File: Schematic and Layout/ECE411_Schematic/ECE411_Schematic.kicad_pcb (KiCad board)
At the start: 2 copper layers, 65 x 56 mm, 13 parts, among them J1 Raspberry Pi GPIO, M1 Motor_DC, U2 PCF8574, U3 LM386, U4 L293D Driver

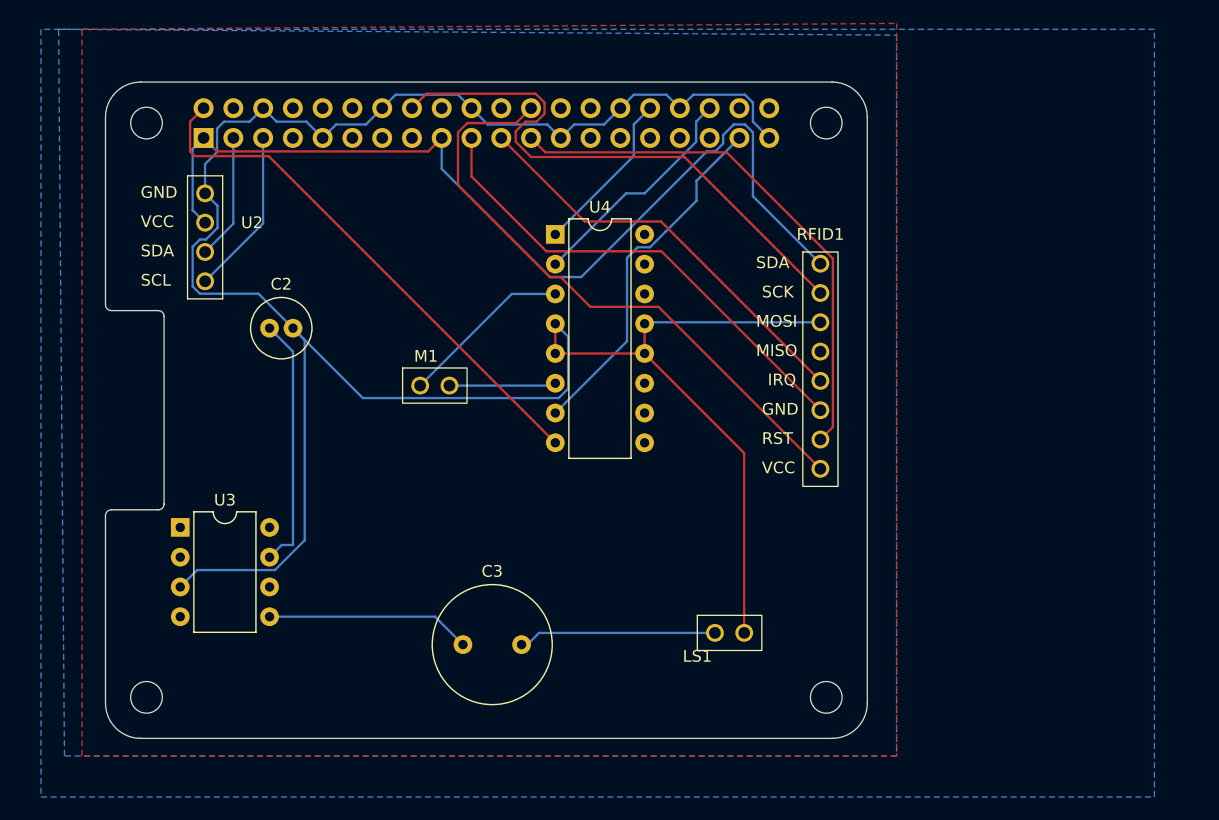
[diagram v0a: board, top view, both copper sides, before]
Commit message: added LEDs to indicate functioning subsystems
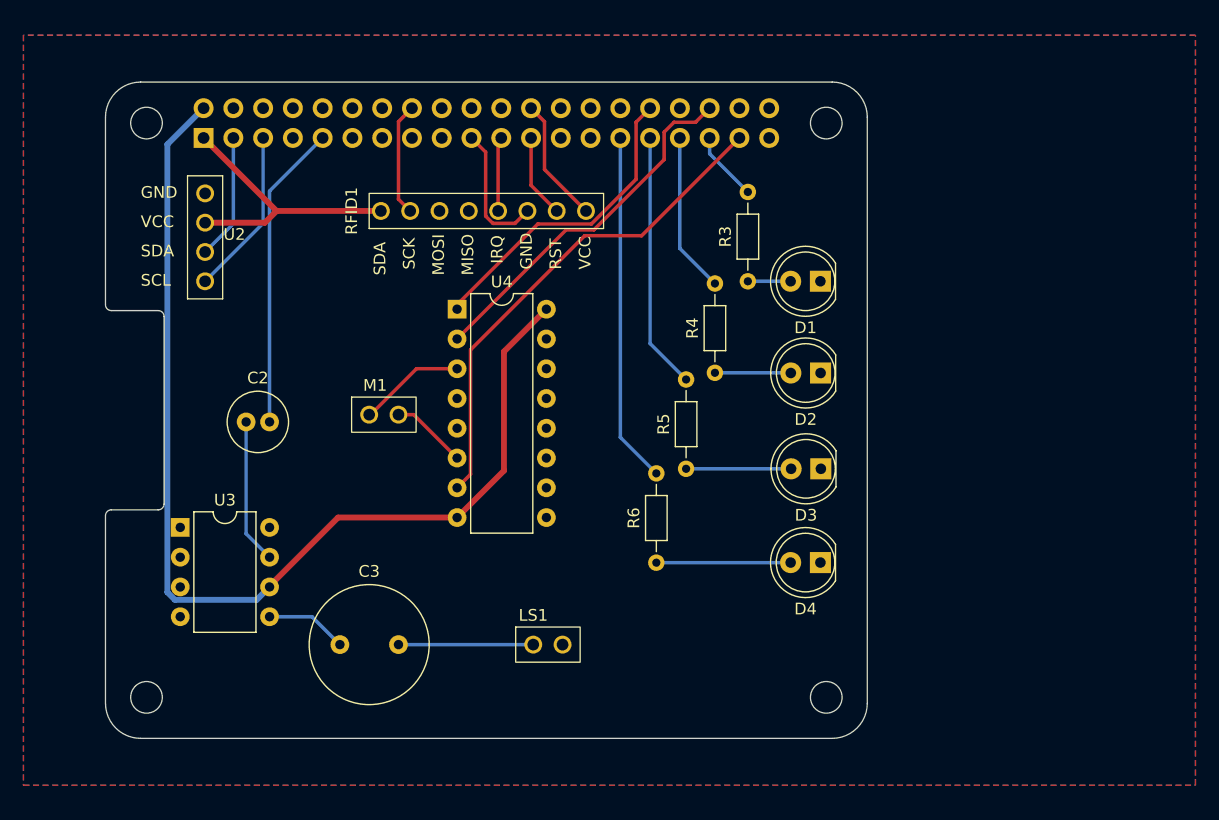
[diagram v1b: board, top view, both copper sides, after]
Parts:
- added D1: RFID LED, LED_THT:LED_D5.0mm, F.Cu at (161.0, 61.0)
- added D2: Motor LED, LED_THT:LED_D5.0mm, F.Cu at (161.0, 68.8)
- added D3: Speaker LED, LED_THT:LED_D5.0mm, F.Cu at (161.0, 77.0)
- added D4: Display LED, LED_THT:LED_D5.0mm, F.Cu at (161.0, 85.0)
- added R3: 220, Resistor_THT:R_Axial_DIN0204_L3.6mm_D1.6mm_P7.62mm_Horizontal, F.Cu at (154.8, 61.0)
- added R4: 220, Resistor_THT:R_Axial_DIN0204_L3.6mm_D1.6mm_P7.62mm_Horizontal, F.Cu at (152.0, 68.8)
- added R5: 220, Resistor_THT:R_Axial_DIN0204_L3.6mm_D1.6mm_P7.62mm_Horizontal, F.Cu at (149.5, 77.0)
- added R6: 220, Resistor_THT:R_Axial_DIN0204_L3.6mm_D1.6mm_P7.62mm_Horizontal, F.Cu at (147.0, 85.0)
- moved RFID1 26.4 mm to (142.5, 57.5), turned to 90 degrees
- moved LS1 15.5 mm to (135.0, 93.5)
- moved U4 10.5 mm to (130.0, 63.4)
- moved C3 10.5 mm to (120.0, 92.0)
- moved C2 8.25 mm to (112.0, 73.0)
- moved M1 5.01 mm to (121.0, 73.9)
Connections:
- J1 pad 29: unconnected-(J1-Pin_29-Pad29) -> Net-(J1-Pin_29)
- J1 pad 31: unconnected-(J1-Pin_31-Pad31) -> Net-(J1-Pin_31)
- J1 pad 33: unconnected-(J1-Pin_33-Pad33) -> Net-(J1-Pin_33)
- J1 pad 35: unconnected-(J1-Pin_35-Pad35) -> Net-(J1-Pin_35)
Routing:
- net GND: track 200.6 -> 26.2 mm
- net +3V3: track 82.0 -> 24.2 mm
- net +5V: track 45.6 -> 91.5 mm
- net /GPIO8/SPI0.CE0: track 52.5 -> 10.7 mm
- net /GPIO11/SPI0.SCLK: track 45.9 -> 7.14 mm
- net /GPIO23: track 48.4 -> 9.66 mm
- net Net-(J1-Pin_29): track 0.00 -> 29.9 mm
- net /GPIO10/SPI0.MOSI: track 41.3 -> 11.4 mm
- net /GPIO9/SPI0.MISO: track 35.8 -> 6.34 mm
- net Net-(J1-Pin_31): track 0.00 -> 21.9 mm
- net Net-(J1-Pin_33): track 0.00 -> 13.7 mm
- net /GPIO12/PWM0: track 14.1 -> 26.7 mm
- net Net-(J1-Pin_37): track 30.6 -> 42.7 mm
- net Net-(D4-A): track 0.00 -> 11.5 mm
- net /GPIO16: track 19.7 -> 31.1 mm
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- added copper zone on F.Cu, net GND
- removed copper zone on F.Cu, net +5V

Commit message: Version 5 schematic and layout
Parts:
- added JP2: Test_point, Resistor_THT:R_Axial_DIN0204_L3.6mm_D1.6mm_P2.54mm_Vertical, F.Cu at (113.4, 58.4)
- added JP3: Test_point, Resistor_THT:R_Axial_DIN0204_L3.6mm_D1.6mm_P2.54mm_Vertical, F.Cu at (115.0, 61.0)
- added JP5: Test_point, Resistor_THT:R_Axial_DIN0204_L3.6mm_D1.6mm_P2.54mm_Vertical, F.Cu at (123.0, 51.8)
- added JP6: Test_point, Resistor_THT:R_Axial_DIN0204_L3.6mm_D1.6mm_P2.54mm_Vertical, F.Cu at (125.0, 68.5)
- added JP7: Test_point, Resistor_THT:R_Axial_DIN0204_L3.6mm_D1.6mm_P2.54mm_Vertical, F.Cu at (125.8, 81.2)
- added JP8: Test_point, Resistor_THT:R_Axial_DIN0204_L3.6mm_D1.6mm_P2.54mm_Vertical, F.Cu at (106.7, 74.4)
- added JP9: Test_point, Resistor_THT:R_Axial_DIN0204_L3.6mm_D1.6mm_P2.54mm_Vertical, F.Cu at (111.6, 54.8)
- added RV1: 10k, Potentiometer_THT:Potentiometer_Bourns_3299W_Vertical, F.Cu at (139.7, 88.3)
- D1, D2, D3, D4: footprint LED_THT:LED_D5.0mm -> LED_SMD:LED_Yuji_5730
- R3, R4, R5, R6: footprint Resistor_THT:R_Axial_DIN0204_L3.6mm_D1.6mm_P7.62mm_Horizontal -> Resistor_SMD:R_0805_2012Metric_Pad1.20x1.40mm_HandSolder
- moved LS1 23.2 mm to (112.3, 98.3)
- moved R6 4.00 mm to (151.0, 85.0), turned to 180 degrees
- moved C3 3.62 mm to (122.8, 89.7)
- moved R5 2.61 mm to (152.2, 77.0), turned to 180 degrees
- moved R3 1.76 mm to (153.1, 61.0), turned to 180 degrees
- moved R4 0.45 mm to (152.4, 68.8), turned to 180 degrees
- moved D1 0.05 mm to (161.1, 61.0)
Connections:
- M1 pad 1: Net-(M1-+) -> Net-(JP6-B)
- RFID1 pad 8: +3V3 -> Net-(JP5-A)
- U2 pad 14: Net-(J1-Pin_5) -> Net-(JP3-B)
- U2 pad 15: Net-(J1-Pin_3) -> Net-(JP2-A)
- U2 pad 16: +3V3 -> Net-(JP9-A)
- U3 pad 3: GND -> Net-(U3-+)
- U3 pad 6: +5V -> Net-(JP8-A)
- U4 pad 16: +5V -> Net-(JP7-A)
- U4 pad 3: Net-(M1-+) -> Net-(JP6-A)
- U4 pad 8: +5V -> Net-(JP7-A)
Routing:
- net +5V: track 91.5 -> 51.6 mm
- net Net-(U3-+): track 0.00 -> 28.7 mm
- net Net-(JP7-A): track 0.00 -> 25.1 mm
- net Net-(JP8-A): track 0.00 -> 15.7 mm
- net Net-(M1-+): track 9.12 -> 0.00 mm
- net (no net): track 0.00 -> 9.12 mm
- net Net-(J1-Pin_29): track 29.9 -> 38.7 mm
- net Net-(J1-Pin_31): track 21.9 -> 30.2 mm
- net Net-(J1-Pin_33): track 13.7 -> 21.1 mm
- net Net-(J1-Pin_35): track 5.96 -> 12.4 mm
- net +3V3: track 24.2 -> 18.2 mm
- net Net-(C3-Pad2): track 11.5 -> 17.0 mm
- net Net-(D4-A): track 11.5 -> 6.18 mm
- net Net-(JP2-A): track 0.00 -> 5.08 mm
- net Net-(JP6-A): track 0.00 -> 4.95 mm
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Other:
- board text added: "Audio"

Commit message: Version 6 schematic and Version 4 Layout
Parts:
- added C4: 100u, Capacitor_SMD:C_0805_2012Metric_Pad1.18x1.45mm_HandSolder, F.Cu at (111.8, 58.3)
- added C5: 100u, Capacitor_SMD:C_0805_2012Metric_Pad1.18x1.45mm_HandSolder, F.Cu at (117.5, 75.8)
- added C6: 0.1u, Capacitor_SMD:C_0805_2012Metric_Pad1.18x1.45mm_HandSolder, F.Cu at (114.4, 55.6)
- added C7: 0.1u, Capacitor_SMD:C_0805_2012Metric_Pad1.18x1.45mm_HandSolder, F.Cu at (117.5, 79.2)
- moved JP3 6.15 mm to (118.1, 66.3)
- moved JP2 5.40 mm to (117.1, 62.3)
- moved RV1 2.48 mm to (139.7, 90.8)
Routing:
- net +5V: track 51.6 -> 62.3 mm
- net (no net): track 9.12 -> 0.00 mm
- net Net-(J1-Pin_5): track 14.9 -> 23.2 mm
- net +3V3: track 18.2 -> 25.9 mm
- net Net-(J1-Pin_3): track 11.7 -> 18.5 mm
- net Net-(JP2-A): track 5.08 -> 10.7 mm
- net Net-(JP3-B): track 3.96 -> 9.28 mm
- net GND: track 26.1 -> 30.2 mm, vias 0 -> 27
- net Net-(D3-A): track 5.04 -> 7.54 mm
- net Net-(D2-A): track 4.75 -> 7.25 mm
- net Net-(D4-A): track 6.18 -> 8.66 mm
- net Net-(U3-+): track 28.7 -> 29.8 mm
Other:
- board text added: "ECE 411 Team 16 RFID Spotify Record Player Version 4"
- board text removed: "Extend PCB edge 0.5mm if using SMT header"

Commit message: Final layout and schematic
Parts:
- moved M1 24.9 mm to (142.2, 86.9), turned to 90 degrees
- moved JP6 18.1 mm to (131.5, 85.4), turned to 0 degrees
- moved C5 9.02 mm to (126.3, 73.8)
- moved C7 8.97 mm to (126.3, 77.5)
- moved R6 3.15 mm to (154.2, 85.0)
- moved LS1 1.64 mm to (110.7, 98.7)
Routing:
- net Net-(JP6-A): track 4.95 -> 19.7 mm
- net Net-(M1--): track 6.53 -> 18.4 mm
- net +3V3: track 25.9 -> 35.4 mm
- net Net-(D4-A): track 8.66 -> 5.53 mm
- net Net-(JP6-B): track 4.05 -> 6.68 mm
- net Net-(J1-Pin_29): track 38.7 -> 40.5 mm
- net Net-(C3-Pad2): track 17.0 -> 18.7 mm
- net +5V: track 62.3 -> 63.4 mm
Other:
- board text added: "+"
- board text added: "-"
- board text added: "ECE 411 | Team 16 | RFID Spotify Record Player | Version 5 | 11/20/24"
- board text removed: "ECE 411 Team 16 RFID Spotify Record Player Version 4"
